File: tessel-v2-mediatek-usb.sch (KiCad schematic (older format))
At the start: 49 parts, among them J901 USB_A_2_stack, J902 USB_A_2_stack, U201 MT7620N, U901 AIC1528-0PSTR, U902 AIC1528-0PSTR, U903 FE1.1, X901 12MHz

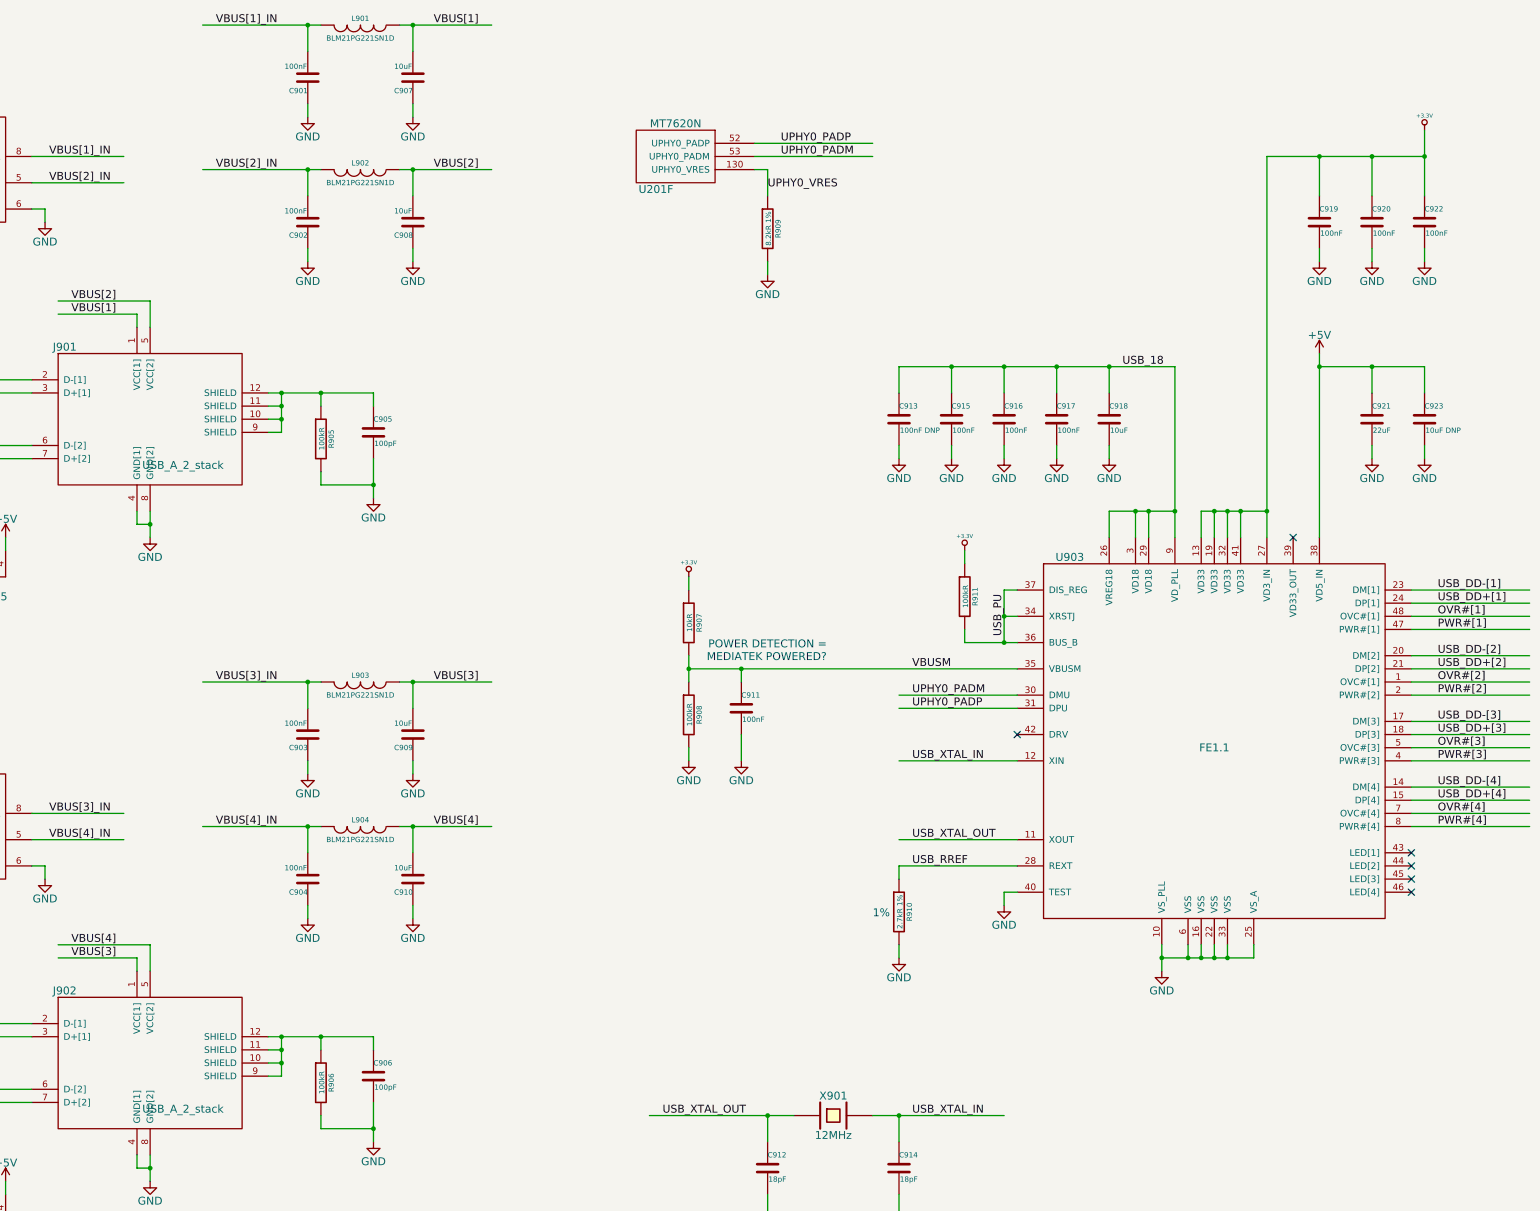
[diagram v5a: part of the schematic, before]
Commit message: value optimization for the sake of bom complexity
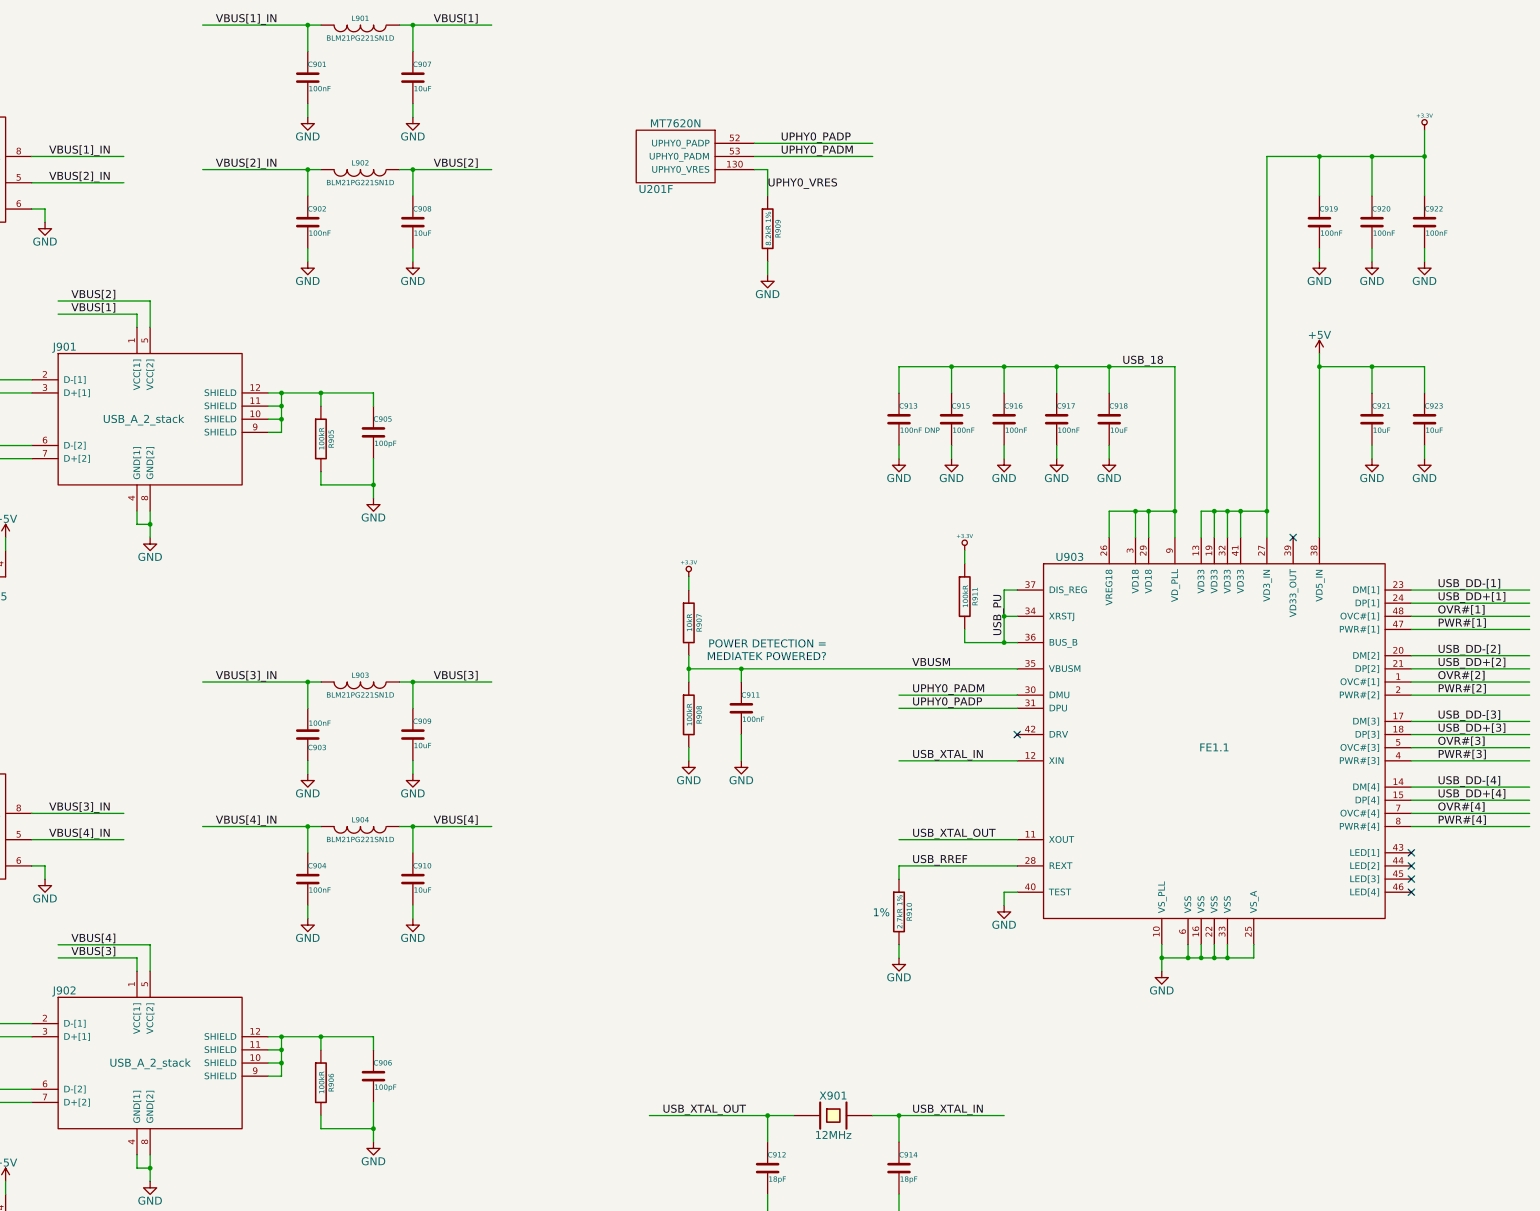
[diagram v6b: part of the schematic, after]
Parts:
- C921: value 22uF -> 10uF
- C923: value 10uF DNP -> 10uF
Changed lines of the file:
@@
 F 3 "" H 6200 7400 60  0000 C CNN
 	1    6200 7400
-	-1   0    0    1
+	1    0    0    -1
 $EndComp
 $Comp
@@
 F 3 "" H 7000 7400 60  0000 C CNN
 	1    7000 7400
-	-1   0    0    1
+	1    0    0    -1
 $EndComp
 Text Label 4400 3100 0    60   ~ 0
@@
 P 14300 3900
 F 0 "C921" H 14300 4000 40  0000 L CNN
-F 1 "22uF" H 14306 3815 40  0000 L CNN
+F 1 "10uF" H 14306 3815 40  0000 L CNN
 F 2 "SMD_Packages:SMD-0805" H 14338 3750 30  0001 C CNN
 F 3 "http://www.digikey.com/product-detail/en/CL21A226MQQNNNE/1276-1100-1-ND/3889186" H 14300 3900 60  0001 C CNN
@@
 P 14700 3900
 F 0 "C923" H 14700 4000 40  0000 L CNN
-F 1 "10uF DNP" H 14706 3815 40  0000 L CNN
+F 1 "10uF" H 14706 3815 40  0000 L CNN
 F 2 "SMD_Packages:SMD-0805" H 14738 3750 30  0001 C CNN
 F 3 "" H 14700 3900 60  0000 C CNN
@@
 F 3 "" H 6200 6300 60  0000 C CNN
 	1    6200 6300
-	-1   0    0    1
+	1    0    0    1
 $EndComp
 $Comp
@@
 F 3 "" H 7000 6300 60  0000 C CNN
 	1    7000 6300
-	-1   0    0    1
+	1    0    0    -1
 $EndComp
 $Comp
@@
 F 3 "" H 6200 2400 60  0000 C CNN
 	1    6200 2400
-	-1   0    0    1
+	1    0    0    -1
 $EndComp
 $Comp
@@
 F 3 "" H 7000 2400 60  0000 C CNN
 	1    7000 2400
-	-1   0    0    1
+	1    0    0    -1
 $EndComp
 $Comp
@@
 F 3 "" H 6200 1300 60  0000 C CNN
 	1    6200 1300
-	-1   0    0    1
+	1    0    0    -1
 $EndComp
 $Comp
@@
 F 3 "" H 7000 1300 60  0000 C CNN
 	1    7000 1300
-	-1   0    0    1
+	1    0    0    -1
 $EndComp
 $Comp
@@
 P 5000 8800
 F 0 "J902" H 4350 9350 60  0000 C CNN
-F 1 "USB_A_2_stack" H 5250 8450 60  0000 C CNN
+F 1 "USB_A_2_stack" H 5000 8800 60  0000 C CNN
 F 2 "tm-kicad-lib:USB-double-xx-UAF-28" H 5800 9300 60  0001 C CNN
 F 3 "" H 5800 9300 60  0000 C CNN
@@
 P 5000 3900
 F 0 "J901" H 4350 4450 60  0000 C CNN
-F 1 "USB_A_2_stack" H 5250 3550 60  0000 C CNN
+F 1 "USB_A_2_stack" H 4950 3900 60  0000 C CNN
 F 2 "tm-kicad-lib:USB-double-xx-UAF-28" H 5800 4400 60  0001 C CNN
 F 3 "" H 5800 4400 60  0000 C CNN

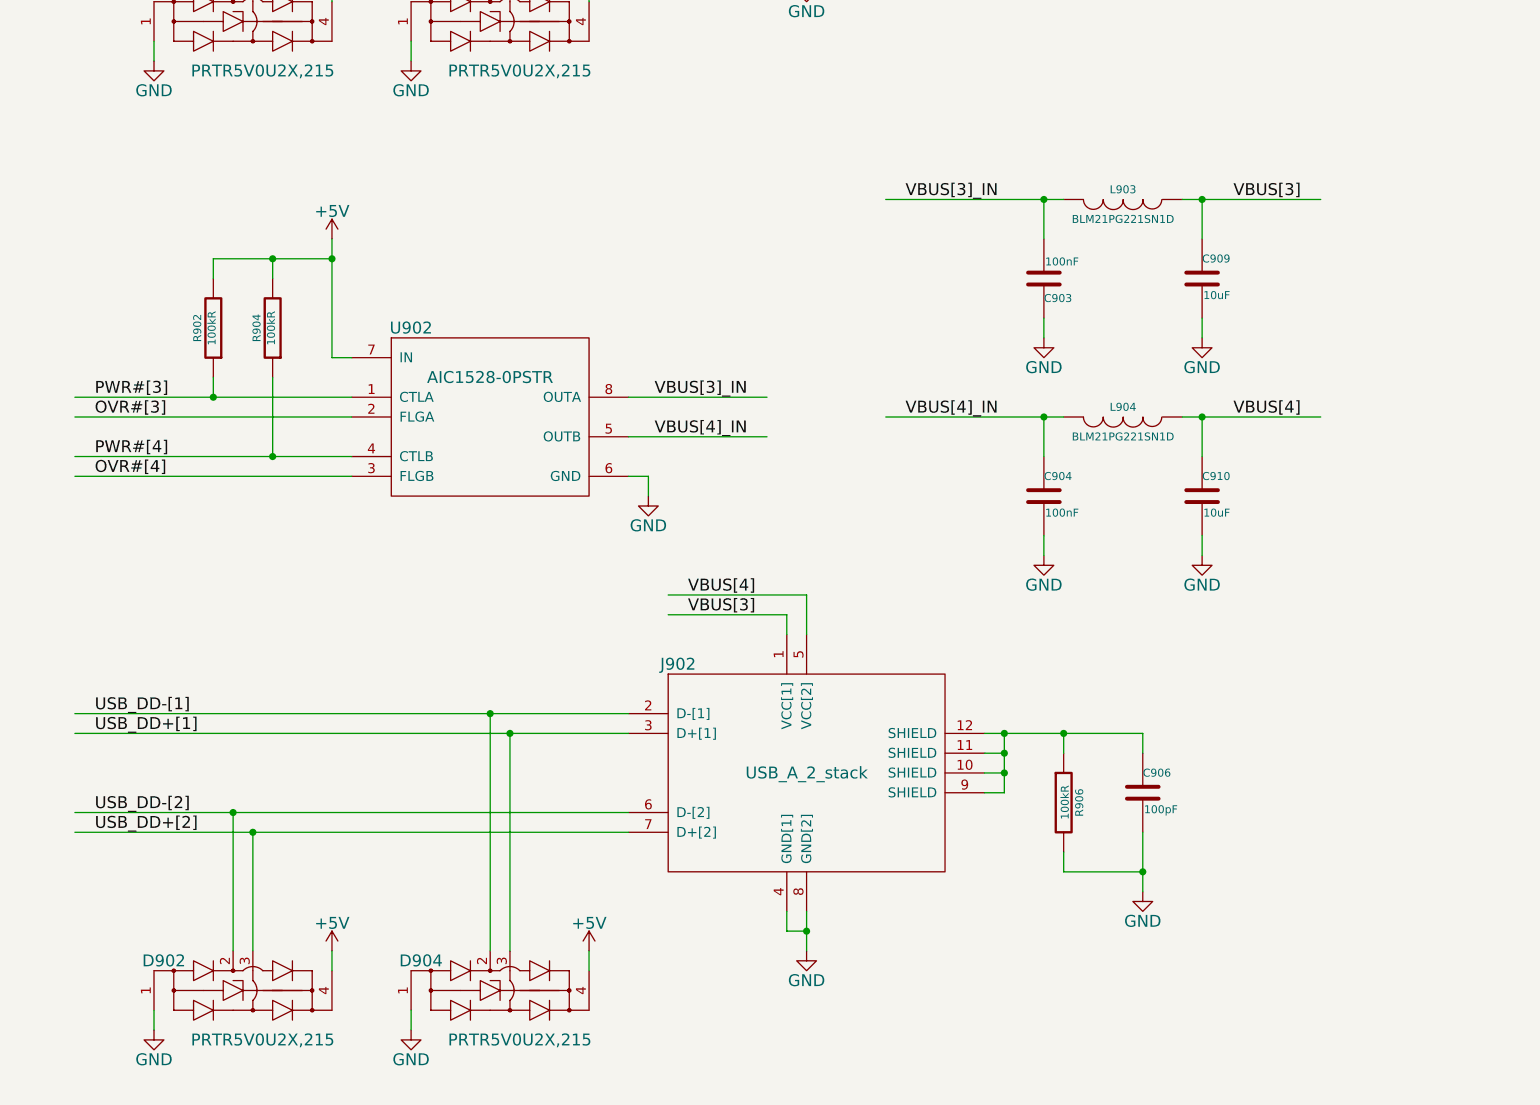
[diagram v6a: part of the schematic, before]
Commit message: tagged 2 usb ports as optional
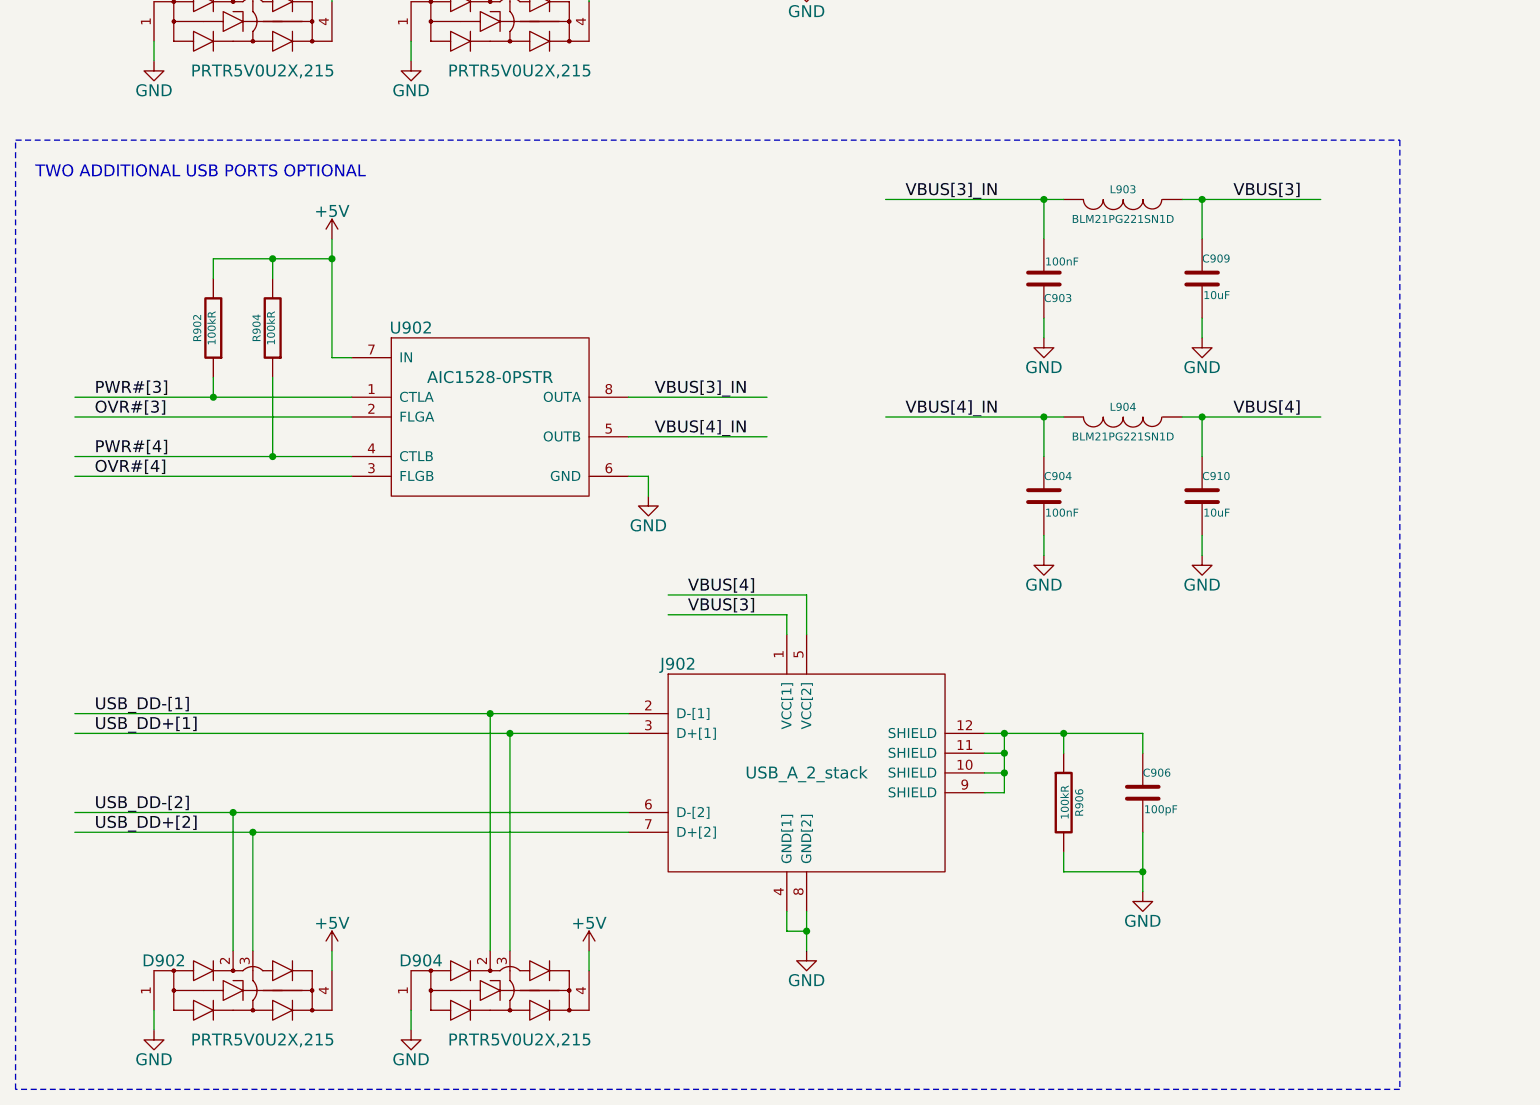
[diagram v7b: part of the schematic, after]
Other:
- note added: "TWO ADDITIONAL USB PORTS OPTIONAL"
